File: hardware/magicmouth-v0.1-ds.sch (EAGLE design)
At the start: 33 parts, among them IC1 LM386N, IC2 ATMEGA168-20P, Q1 16Mhz, U1 ARDUINOR3-NOIOREF-NOTEXT

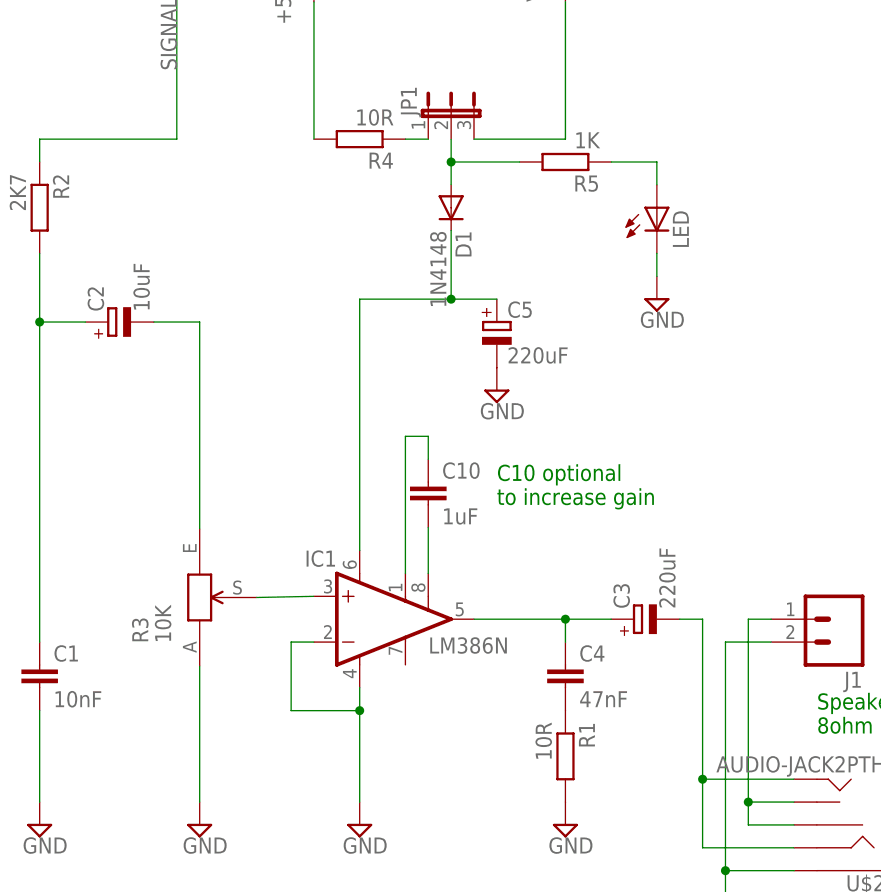
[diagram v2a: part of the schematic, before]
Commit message: 220K resistor in series with gain control
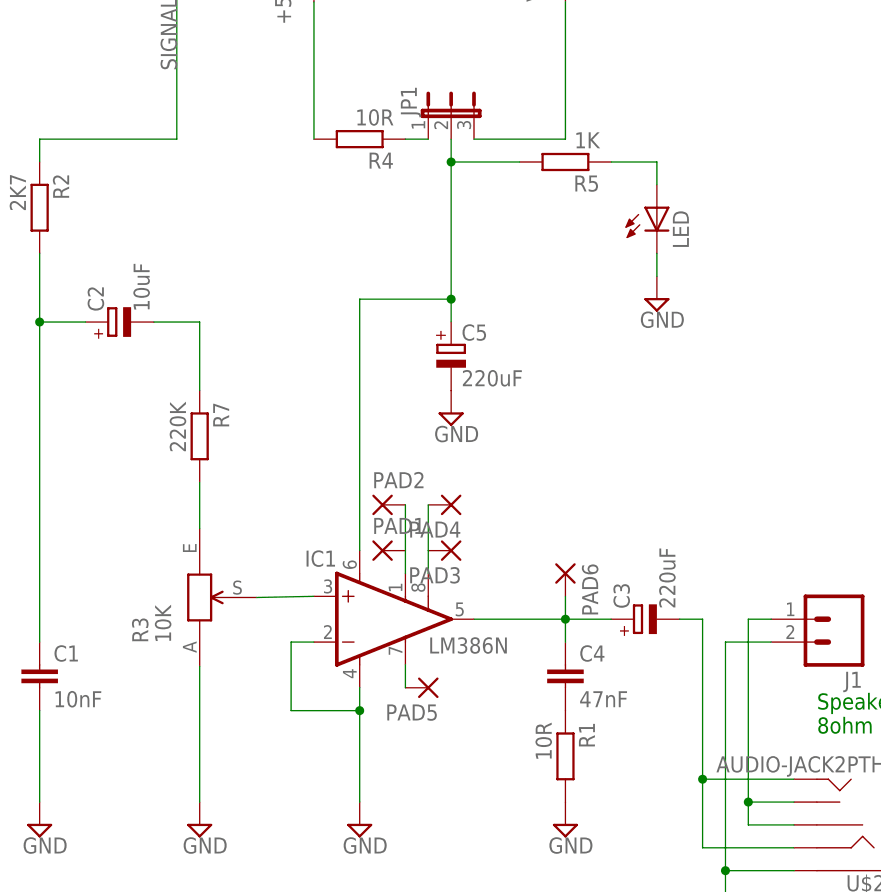
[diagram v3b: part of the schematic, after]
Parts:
- removed C10: 1uF, rcl:C-EU050-025X075
- removed D1: 1N4148, diode:1N4148DO35-7
- added PAD1, PAD2, PAD3, PAD4, PAD5, PAD6: (no value), wirepad:1,6/0,8
- added R7: 220K, resistor:R-EU_0207/7
- JP2: device adafruit:PINHD-1X8BIG -> adafruit:PINHD-1X8CLEANBIG
- JP4: device adafruit:PINHD-1X6B -> adafruit:PINHD-1X6CB
- R2: device resistor:R-EU_0207/10 -> rcl:R-EU_0207/7
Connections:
- removed net N$27: D1.A, JP1.2, R5.2
- removed net N$98: C10.1, IC1.GAIN@1
- removed net N$99: C10.2, IC1.GAIN@2
- new net N$101: IC1.GAIN@2, PAD3.P, PAD4.P
- new net N$58: IC1.GAIN@1, PAD1.P, PAD2.P
- new net N$87: C2.-, R7.1
- new net N$94: IC1.BYPASS, PAD5.P
- net N$1: now also PAD6.P
- net N$5: now also R7.2; no longer C2.-
- net VS: now also JP1.2, R5.2; no longer D1.C
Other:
- note removed: "C10 optional to increase gain"
- moved on the sheet: C5
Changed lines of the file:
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@@
 <part name="IC1" library="linear" deviceset="LM386?-*" device="N" technology="1" value="LM386N"/>
 <part name="R1" library="resistor" deviceset="R-EU_" device="0207/7" value="10R"/>
-<part name="R2" library="resistor" deviceset="R-EU_" device="0207/10" value="2K7"/>
+<part name="R2" library="rcl" deviceset="R-EU_" device="0207/7" value="2K7"/>
 <part name="GND1" library="supply2" deviceset="GND" device=""/>
 <part name="C1" library="rcl" deviceset="C-EU" device="050-025X075" value="10nF"/>
@@
 <part name="GND3" library="supply2" deviceset="GND" device=""/>
 <part name="JP1" library="jumper" deviceset="JP2E" device=""/>
-<part name="D1" library="diode" deviceset="1N4148" device="DO35-7" value="1N4148"/>
 <part name="R5" library="rcl" deviceset="R-EU_" device="0207/7" value="1K"/>
 <part name="LED" library="led" deviceset="LED" device="3MM"/>
@@
 <part name="GND12" library="supply2" deviceset="GND1" device=""/>
 <part name="GND13" library="supply2" deviceset="GND1" device=""/>
-<part name="JP2" library="adafruit" deviceset="PINHD-1X8" device="BIG"/>
+<part name="JP2" library="adafruit" deviceset="PINHD-1X8" device="CLEANBIG"/>
 <part name="P+1" library="supply1" deviceset="VCC" device=""/>
 <part name="P+2" library="supply1" deviceset="VCC" device=""/>
 <part name="GND14" library="supply2" deviceset="GND" device=""/>
-<part name="JP4" library="adafruit" deviceset="PINHD-1X6" device="B"/>
+<part name="JP4" library="adafruit" deviceset="PINHD-1X6" device="CB"/>
 <part name="J1" library="SparkFun-Connectors" deviceset="M02" device="3.5MM"/>
 <part name="P+5" library="supply1" deviceset="+5V" device=""/>
@@
 <part name="JP8" library="SparkFun-Passives" deviceset="JUMPER-2" device="PTH"/>
 <part name="U$2" library="SparkFun-Connectors" deviceset="AUDIO-JACK2" device="PTH"/>
-<part name="C10" library="rcl" deviceset="C-EU" device="050-025X075" value="1uF">
-<attribute name="CAPACITANCE" value="22 pf"/>
-</part>
 <part name="JP9" library="SparkFun-Connectors" deviceset="M01" device="SMDNS"/>
+<part name="R7" library="resistor" deviceset="R-EU_" device="0207/7" value="220K"/>
+<part name="PAD1" library="wirepad" deviceset="1,6/0,8" device=""/>
+<part name="PAD2" library="wirepad" deviceset="1,6/0,8" device=""/>
+<part name="PAD3" library="wirepad" deviceset="1,6/0,8" device=""/>
+<part name="PAD4" library="wirepad" deviceset="1,6/0,8" device=""/>
+<part name="PAD5" library="wirepad" deviceset="1,6/0,8" device=""/>
+<part name="PAD6" library="wirepad" deviceset="1,6/0,8" device=""/>
 </parts>
 <sheets>
@@
 <text x="109.22" y="27.94" size="1.778" layer="91">3.5mm headphone
 jack socket</text>
-<text x="73.66" y="76.2" size="1.778" layer="91">C10 optional
-to increase gain</text>
 </plain>
 <instances>
@@
 <instance part="GND6" gate="GND" x="99.06" y="25.4"/>
 <instance part="R4" gate="G$1" x="58.42" y="116.84" rot="R180"/>
-<instance part="C5" gate="G$1" x="73.66" y="96.52"/>
-<instance part="GND3" gate="GND" x="73.66" y="88.9"/>
+<instance part="C5" gate="G$1" x="68.58" y="93.98"/>
+<instance part="GND3" gate="GND" x="68.58" y="86.36"/>
 <instance part="JP1" gate="1" x="68.58" y="119.38"/>
-<instance part="D1" gate="G$1" x="68.58" y="109.22" rot="R270"/>
 <instance part="R5" gate="G$1" x="81.28" y="114.3" rot="R180"/>
 <instance part="LED" gate="G$1" x="91.44" y="109.22"/>
@@
 <instance part="JP8" gate="A" x="276.86" y="38.1"/>
 <instance part="U$2" gate="G$1" x="111.76" y="40.64" rot="R180"/>
-<instance part="C10" gate="G$1" x="66.04" y="78.74"/>
 <instance part="JP9" gate="G$1" x="254" y="58.42" rot="R90"/>
+<instance part="R7" gate="G$1" x="40.64" y="83.82" rot="R270"/>
+<instance part="PAD1" gate="P" x="60.96" y="71.12"/>
+<instance part="PAD2" gate="P" x="60.96" y="76.2"/>
+<instance part="PAD3" gate="P" x="68.58" y="71.12" rot="R180"/>
+<instance part="PAD4" gate="P" x="68.58" y="76.2" rot="R180"/>
+<instance part="PAD5" gate="P" x="66.04" y="55.88" rot="R180"/>
+<instance part="PAD6" gate="P" x="81.28" y="68.58" rot="R270"/>
 </instances>
 <busses>
@@
 <net name="N$5" class="0">
 <segment>
-<wire x1="35.56" y1="96.52" x2="40.64" y2="96.52" width="0.1524" layer="91"/>
-<pinref part="C2" gate="G$1" pin="-"/>
 <pinref part="R3" gate="G$1" pin="E"/>
-<wire x1="40.64" y1="73.533" x2="40.64" y2="96.52" width="0.1524" layer="91"/>
+<wire x1="40.64" y1="73.533" x2="40.64" y2="78.74" width="0.1524" layer="91"/>
+<pinref part="R7" gate="G$1" pin="2"/>
 </segment>
 </net>
@@
 <pinref part="C3" gate="G$1" pin="+"/>
 <pinref part="C4" gate="G$1" pin="1"/>
+<pinref part="PAD6" gate="P" pin="P"/>
+<wire x1="81.28" y1="63.5" x2="81.28" y2="66.04" width="0.1524" layer="91"/>
 </segment>
 </net>
@@
 <segment>
 <wire x1="58.42" y1="71.12" x2="58.42" y2="99.06" width="0.1524" layer="91"/>
-<wire x1="73.66" y1="99.06" x2="68.58" y2="99.06" width="0.1524" layer="91"/>
+<wire x1="68.58" y1="96.52" x2="68.58" y2="99.06" width="0.1524" layer="91"/>
 <wire x1="68.58" y1="99.06" x2="58.42" y2="99.06" width="0.1524" layer="91"/>
-<wire x1="68.58" y1="106.68" x2="68.58" y2="99.06" width="0.1524" layer="91"/>
+<wire x1="68.58" y1="114.3" x2="68.58" y2="99.06" width="0.1524" layer="91"/>
 <junction x="68.58" y="99.06"/>
 <pinref part="IC1" gate="G$1" pin="VS"/>
 <pinref part="C5" gate="G$1" pin="+"/>
-<pinref part="D1" gate="G$1" pin="C"/>
+<pinref part="JP1" gate="1" pin="2"/>
+<pinref part="R5" gate="G$1" pin="2"/>
+<wire x1="68.58" y1="114.3" x2="68.58" y2="116.84" width="0.1524" layer="91"/>
+<wire x1="76.2" y1="114.3" x2="68.58" y2="114.3" width="0.1524" layer="91"/>
+<junction x="68.58" y="114.3"/>
 </segment>
 </net>
@@
 </segment>
 </net>
-<net name="N$27" class="0">
-<segment>
-<wire x1="68.58" y1="111.76" x2="68.58" y2="114.3" width="0.1524" layer="91"/>
-<pinref part="JP1" gate="1" pin="2"/>
-<pinref part="D1" gate="G$1" pin="A"/>
-<pinref part="R5" gate="G$1" pin="2"/>
-<wire x1="68.58" y1="114.3" x2="68.58" y2="116.84" width="0.1524" layer="91"/>
-<wire x1="76.2" y1="114.3" x2="68.58" y2="114.3" width="0.1524" layer="91"/>
-<junction x="68.58" y="114.3"/>
-</segment>
-</net>
 <net name="+3V3" class="0">
 <segment>
@@
 </segment>
 </net>
-<net name="N$98" class="0">
-<segment>
-<pinref part="IC1" gate="G$1" pin="GAIN@1"/>
-<wire x1="63.5" y1="68.58" x2="63.5" y2="83.82" width="0.1524" layer="91"/>
-<pinref part="C10" gate="G$1" pin="1"/>
-<wire x1="63.5" y1="83.82" x2="66.04" y2="83.82" width="0.1524" layer="91"/>
-<wire x1="66.04" y1="83.82" x2="66.04" y2="81.28" width="0.1524" layer="91"/>
-</segment>
-</net>
-<net name="N$99" class="0">
-<segment>
-<pinref part="IC1" gate="G$1" pin="GAIN@2"/>
-<pinref part="C10" gate="G$1" pin="2"/>
-<wire x1="66.04" y1="68.58" x2="66.04" y2="73.66" width="0.1524" layer="91"/>
-</segment>
-</net>
 <net name="N$12" class="0">
 <segment>
@@
 </segment>
 </net>
+<net name="N$87" class="0">
+<segment>
+<pinref part="C2" gate="G$1" pin="-"/>
+<pinref part="R7" gate="G$1" pin="1"/>
+<wire x1="35.56" y1="96.52" x2="40.64" y2="96.52" width="0.1524" layer="91"/>
+<wire x1="40.64" y1="96.52" x2="40.64" y2="88.9" width="0.1524" layer="91"/>
+</segment>
+</net>
+<net name="N$58" class="0">
+<segment>
+<pinref part="PAD2" gate="P" pin="P"/>
+<pinref part="PAD1" gate="P" pin="P"/>
+<wire x1="63.5" y1="76.2" x2="63.5" y2="71.12" width="0.1524" layer="91"/>
+<pinref part="IC1" gate="G$1" pin="GAIN@1"/>
+<wire x1="63.5" y1="71.12" x2="63.5" y2="68.58" width="0.1524" layer="91"/>
+</segment>
+</net>
+<net name="N$101" class="0">
+<segment>
+<pinref part="PAD4" gate="P" pin="P"/>
+<pinref part="PAD3" gate="P" pin="P"/>
+<wire x1="66.04" y1="76.2" x2="66.04" y2="71.12" width="0.1524" layer="91"/>
+<pinref part="IC1" gate="G$1" pin="GAIN@2"/>
+<wire x1="66.04" y1="71.12" x2="66.04" y2="68.58" width="0.1524" layer="91"/>
+</segment>
+</net>
+<net name="N$94" class="0">
+<segment>
+<pinref part="PAD5" gate="P" pin="P"/>
+<pinref part="IC1" gate="G$1" pin="BYPASS"/>
+<wire x1="63.5" y1="55.88" x2="63.5" y2="58.42" width="0.1524" layer="91"/>
+</segment>
+</net>

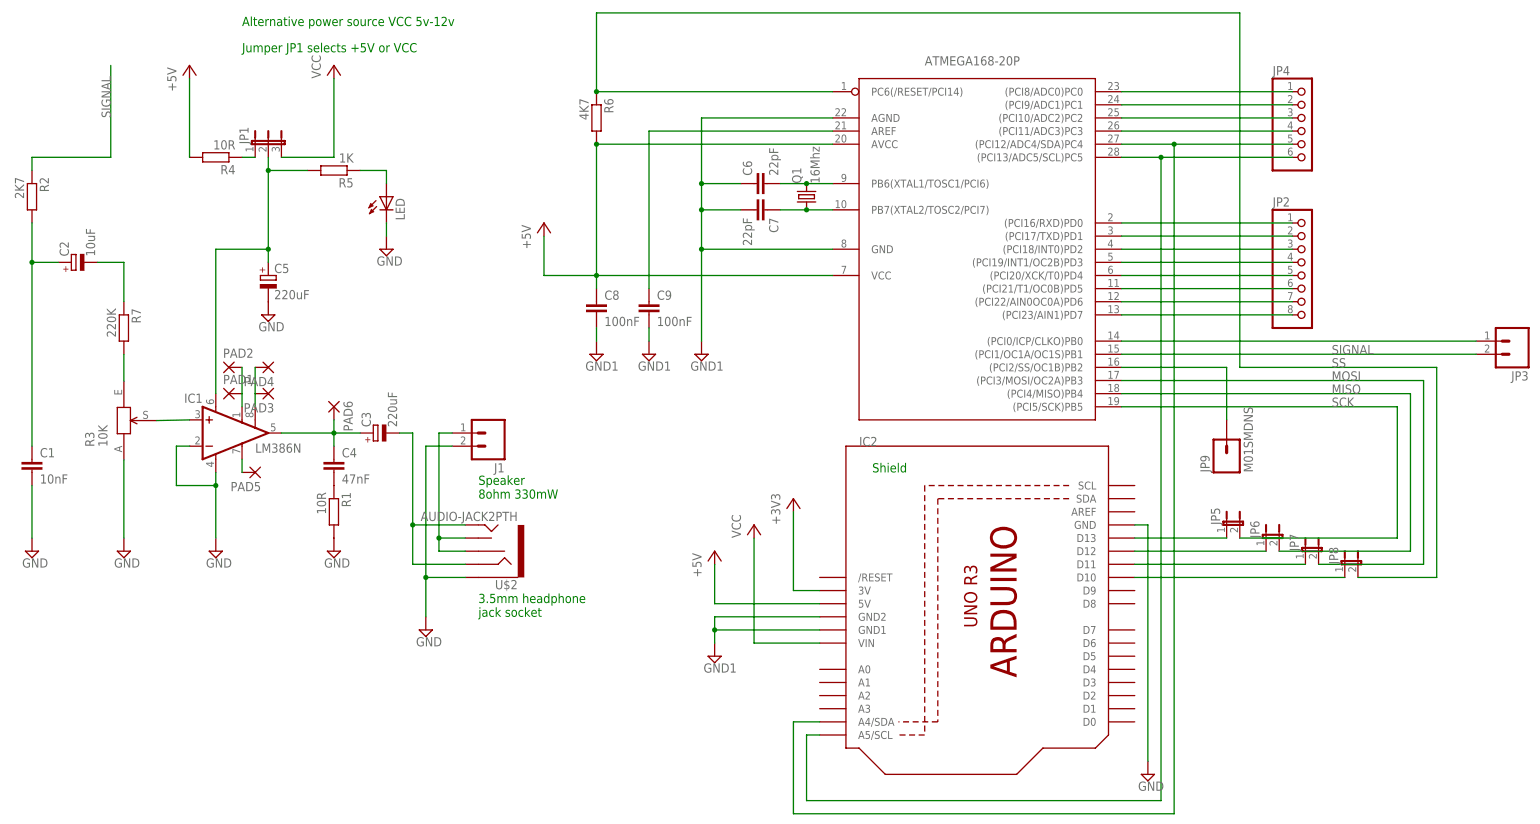
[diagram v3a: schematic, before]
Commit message: vertical 220uF caps, 6 pin IO header
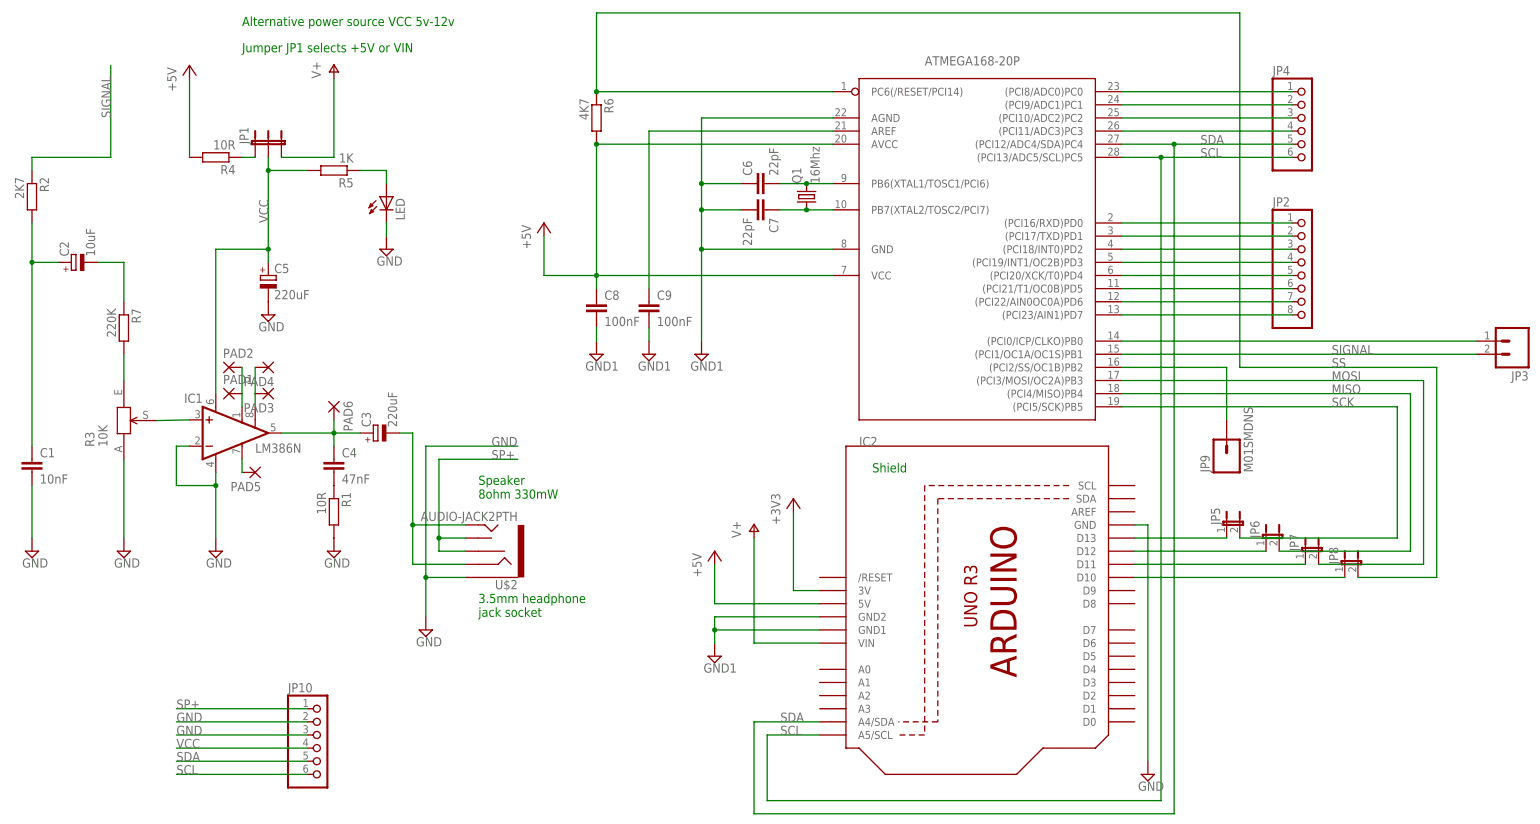
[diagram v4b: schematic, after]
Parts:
- removed J1: (no value), SparkFun-Connectors:M023.5MM
- added JP10: (no value), adafruit:PINHD-1X6CB
- C3, C5: device rcl:CPOL-EUTT5D7L -> rcl:CPOL-EUTT2D7
- JP1: value (none) -> JUMPER-3PTH; device jumper:JP2E -> SparkFun-Passives:JUMPER-3PTH
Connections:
- removed net N$3: J1.1, U$2.RSH, U$2.TSH
- removed net N$30: IC2.(PCI12/ADC4/SDA)PC4, JP4.5, U1.A4/SDA
- removed net N$31: IC2.(PCI13/ADC5/SCL)PC5, JP4.6, U1.A5/SCL
- removed net VS: C5.+, IC1.VS, JP1.2, R5.2
- new net SCL: IC2.(PCI13/ADC5/SCL)PC5, JP10.6, JP4.6, U1.A5/SCL
- new net SDA: IC2.(PCI12/ADC4/SDA)PC4, JP10.5, JP4.5, U1.A4/SDA
- new net SP+: JP10.1, U$2.RSH, U$2.TSH
- new net VIN: JP1.3, U1.VIN
- net GND: now also JP10.2, JP10.3; no longer J1.2
- net VCC: now also C5.+, IC1.VS, JP1.2, JP10.4, R5.2; no longer JP1.3, U1.VIN
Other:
- note added: "Jumper JP1 selects +5V or VIN"
- note removed: "Jumper JP1 selects +5V or VCC"

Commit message: adjusted placement to avoid through holes directly above Arduino USB port
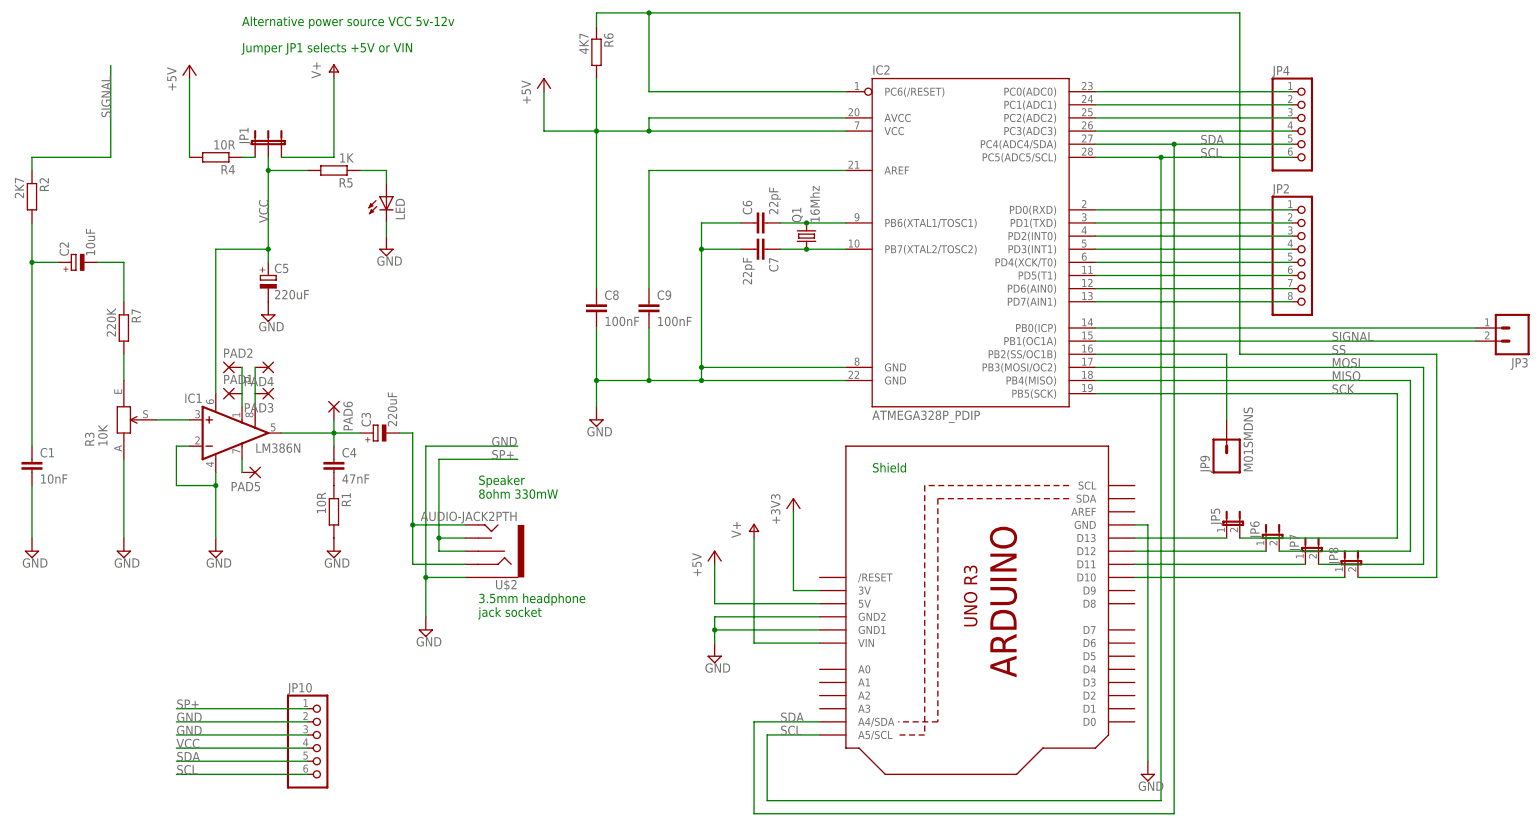
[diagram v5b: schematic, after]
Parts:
- IC2: value ATMEGA168-20P -> ATMEGA328P_PDIP; device adafruit:ATMEGA168-20P -> SparkFun-DigitalIC:ATMEGA328P_PDIP
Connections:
- net GND: now also IC2.GND@1, IC2.GND@2; no longer IC2.AGND, IC2.GND
- net MISO: now also IC2.PB4(MISO); no longer IC2.(PCI4/MISO)PB4
- net MOSI: now also IC2.PB3(MOSI/OC2); no longer IC2.(PCI3/MOSI/OC2A)PB3
- net N$11: now also IC2.PB7(XTAL2/TOSC2); no longer IC2.PB7(XTAL2/TOSC2/PCI7)
- net N$12: now also IC2.PB2(SS/OC1B); no longer IC2.(PCI2/SS/OC1B)PB2
- net N$13: now also IC2.PC0(ADC0); no longer IC2.(PCI8/ADC0)PC0
- net N$15: now also IC2.PC1(ADC1); no longer IC2.(PCI9/ADC1)PC1
- net N$16: now also IC2.PD0(RXD); no longer IC2.(PCI16/RXD)PD0
- net N$17: now also IC2.PD1(TXD); no longer IC2.(PCI17/TXD)PD1
- net N$18: now also IC2.PD2(INT0); no longer IC2.(PCI18/INT0)PD2
- net N$19: now also IC2.PD3(INT1); no longer IC2.(PCI19/INT1/OC2B)PD3
- net N$20: now also IC2.PD4(XCK/T0); no longer IC2.(PCI20/XCK/T0)PD4
- net N$21: now also IC2.PD5(T1); no longer IC2.(PCI21/T1/OC0B)PD5
- net N$22: now also IC2.PD6(AIN0); no longer IC2.(PCI22/AIN0OC0A)PD6
- net N$23: now also IC2.PD7(AIN1); no longer IC2.(PCI23/AIN1)PD7
- net N$24: now also IC2.PB0(ICP); no longer IC2.(PCI0/ICP/CLKO)PB0
- net N$32: now also IC2.PC2(ADC2); no longer IC2.(PCI10/ADC2)PC2
- net N$33: now also IC2.PC3(ADC3); no longer IC2.(PCI11/ADC3)PC3
- net N$6: now also IC2.PB6(XTAL1/TOSC1); no longer IC2.PB6(XTAL1/TOSC1/PCI6)
- net SCK: now also IC2.PB5(SCK); no longer IC2.(PCI5/SCK)PB5
- net SCL: now also IC2.PC5(ADC5/SCL); no longer IC2.(PCI13/ADC5/SCL)PC5
- net SDA: now also IC2.PC4(ADC4/SDA); no longer IC2.(PCI12/ADC4/SDA)PC4
- net SIGNAL: now also IC2.PB1(OC1A); no longer IC2.(PCI1/OC1A/OC1S)PB1
- net SS: now also IC2.PC6(/RESET); no longer IC2.PC6(/RESET/PCI14)
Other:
- moved on the sheet: C6, C7, IC2, JP2, JP3, Q1, R6
